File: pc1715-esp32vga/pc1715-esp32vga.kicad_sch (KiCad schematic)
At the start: 31 parts, among them J1001 IDC10_VIDEO_IN, J1002 VGAOUT, J1003 USB_B, J1004 KEYPAD, J1005 IDC16_VGAOUT, SW1001 RST, U1001 ESP32-S3-WROOM-1, U1002 LM1117MP-3.3

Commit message: Revision 2
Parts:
- removed D1001: 1N5819, Diode_THT:D_DO-41_SOD81_P7.62mm_Horizontal, symbol Diode:1N5819
- removed TP1001: TP_SPI, TestPoint:TestPoint_Pad_1.5x1.5mm, symbol Connector:TestPoint
- removed TP1002: TP_COPY, TestPoint:TestPoint_Pad_1.5x1.5mm, symbol Connector:TestPoint
- added D3: SYNC, LED_SMD:LED_1206_3216Metric_Pad1.42x1.75mm_HandSolder, symbol Device:LED
- added D4: STAT, LED_SMD:LED_1206_3216Metric_Pad1.42x1.75mm_HandSolder, symbol Device:LED
- added J6: USB_C_Receptacle_USB2.0_16P, Connector_USB:USB_C_Receptacle_GCT_USB4105-xx-A_16P_TopMnt_Horizontal, symbol Connector:USB_C_Receptacle_USB2.0_16P
- added J7: DBG, Connector_PinHeader_2.54mm:PinHeader_1x07_P2.54mm_Vertical, symbol Connector:Conn_01x07_Pin
- added R3, R4: 330, Resistor_SMD:R_0805_2012Metric_Pad1.20x1.40mm_HandSolder, symbol Device:R
- D1: renamed from D1002; value 1N5819 -> BAT54C Uf 0,24V; footprint Diode_THT:D_DO-41_SOD81_P7.62mm_Horizontal -> Package_TO_SOT_SMD:SOT-23; symbol Diode:1N5819 -> Diode:BAT54C
- D2: renamed from D1003; value LED -> 3V3
- J4: renamed from J1004; footprint Connector_PinHeader_2.54mm:PinHeader_1x05_P2.54mm_Vertical -> Connector_PinSocket_2.54mm:PinSocket_1x05_P2.54mm_Horizontal
- JP1: renamed from JP1001; footprint Connector_PinSocket_2.54mm:PinSocket_1x02_P2.54mm_Vertical -> Connector_PinHeader_2.54mm:PinHeader_1x02_P2.54mm_Vertical
- R2: renamed from R1001; value 300 -> 330
- renumbered C1001 to C1, C1002 to C2, J1001 to J1, J1002 to J2, J1003 to J3, J1005 to J5, R1010 to R1, R1009 to R10, R1002 to R11, R1003 to R12, R1011 to R13, R1004 to R5, R1005 to R6, R1006 to R7, R1007 to R8, R1008 to R9, SW1001 to SW1, U1002 to U1, U1001 to U2
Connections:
- net +5V: now also D1.3; no longer D1.1 (K)
- net BSYNC: now also J7.7 (Pin_7)
- net GND: now also J6.A1 (GND), J6.A12 (GND), J6.B1 (GND), J6.B12 (GND), J6.S1 (SHIELD), R3.1, R4.1
- net INTENS: now also J7.5 (Pin_5)
- net K_DOWN: now also J4.2 (Pin_2); no longer J4.4 (Pin_4)
- net K_LEFT: now also J4.5 (Pin_5); no longer J4.1 (Pin_1)
- net K_RIGHT: now also J4.1 (Pin_1); no longer J4.5 (Pin_5)
- net K_UP: now also J4.4 (Pin_4); no longer J4.2 (Pin_2)
- net USB_DN: now also J6.A7 (D-), J6.B7 (D-)
- net USB_DP: now also J6.A6 (D+), J6.B6 (D+)
- net VIDEO: now also J7.6 (Pin_6)
- net at U2.16 (GPIO46): now also D3.2 (A)
- net TP_11: now reaches U2.19 (GPIO11/TOUCH11/ADC2_CH0/FSPID/FSPIIO5/SUBSPID)
- net TP_11: now also J7.3 (Pin_3)
- net TP_12: now reaches U2.20 (GPIO12/TOUCH12/ADC2_CH1/FSPICLK/FSPIIO6/SUBSPICLK)
- net TP_12: now also J7.4 (Pin_4)
- net TP_SPI: now reaches U2.21 (GPIO13/TOUCH13/ADC2_CH2/FSPIQ/FSPIIO7/SUBSPIQ)
- net TP_SPI: now also J7.1 (Pin_1)
- net TP_CPY: now reaches U2.22 (GPIO14/TOUCH14/ADC2_CH3/FSPIWP/FSPIDQS/SUBSPIWP)
- net TP_CPY: now also J7.2 (Pin_2)
- net at U2.35 (MTMS/GPIO42): now also D4.2 (A)
- net VBUS: now reaches D1.2, J3.1 (VBUS)
- net VBUS: now also J6.A4 (VBUS), J6.A9 (VBUS), J6.B4 (VBUS), J6.B9 (VBUS)
- net 5V_VID: now reaches J1.1 (Pin_1), J1.2 (Pin_2)
- net 5V_VID: now also D1.1
- new net: D3.1 (K), R3.2
- new net: D4.1 (K), R4.2
- no-connect marks 26 -> 25
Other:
- note added: "Debugging"
- note removed: "A7100 PullUp *OPTIONAL* für PC1715 nicht benötigt"
- moved on the sheet: H1001, H1002, H1003, H1004, J1, J4, R11, R12, R13

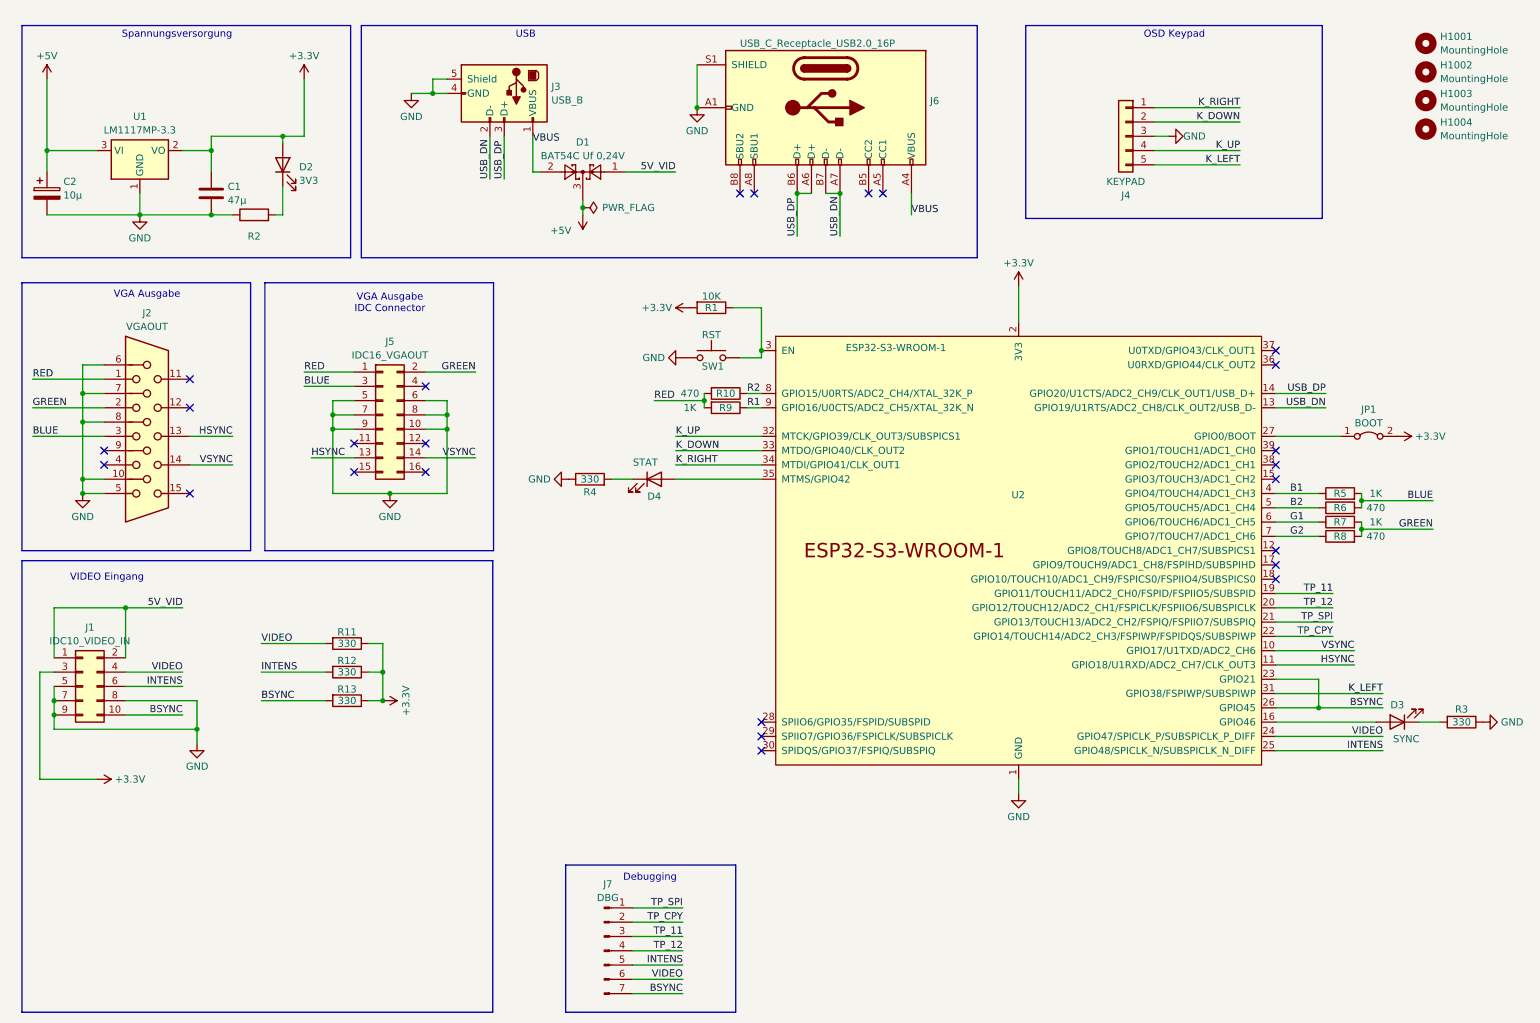
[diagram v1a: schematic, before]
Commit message: Rev 2 Main PCB with keypad
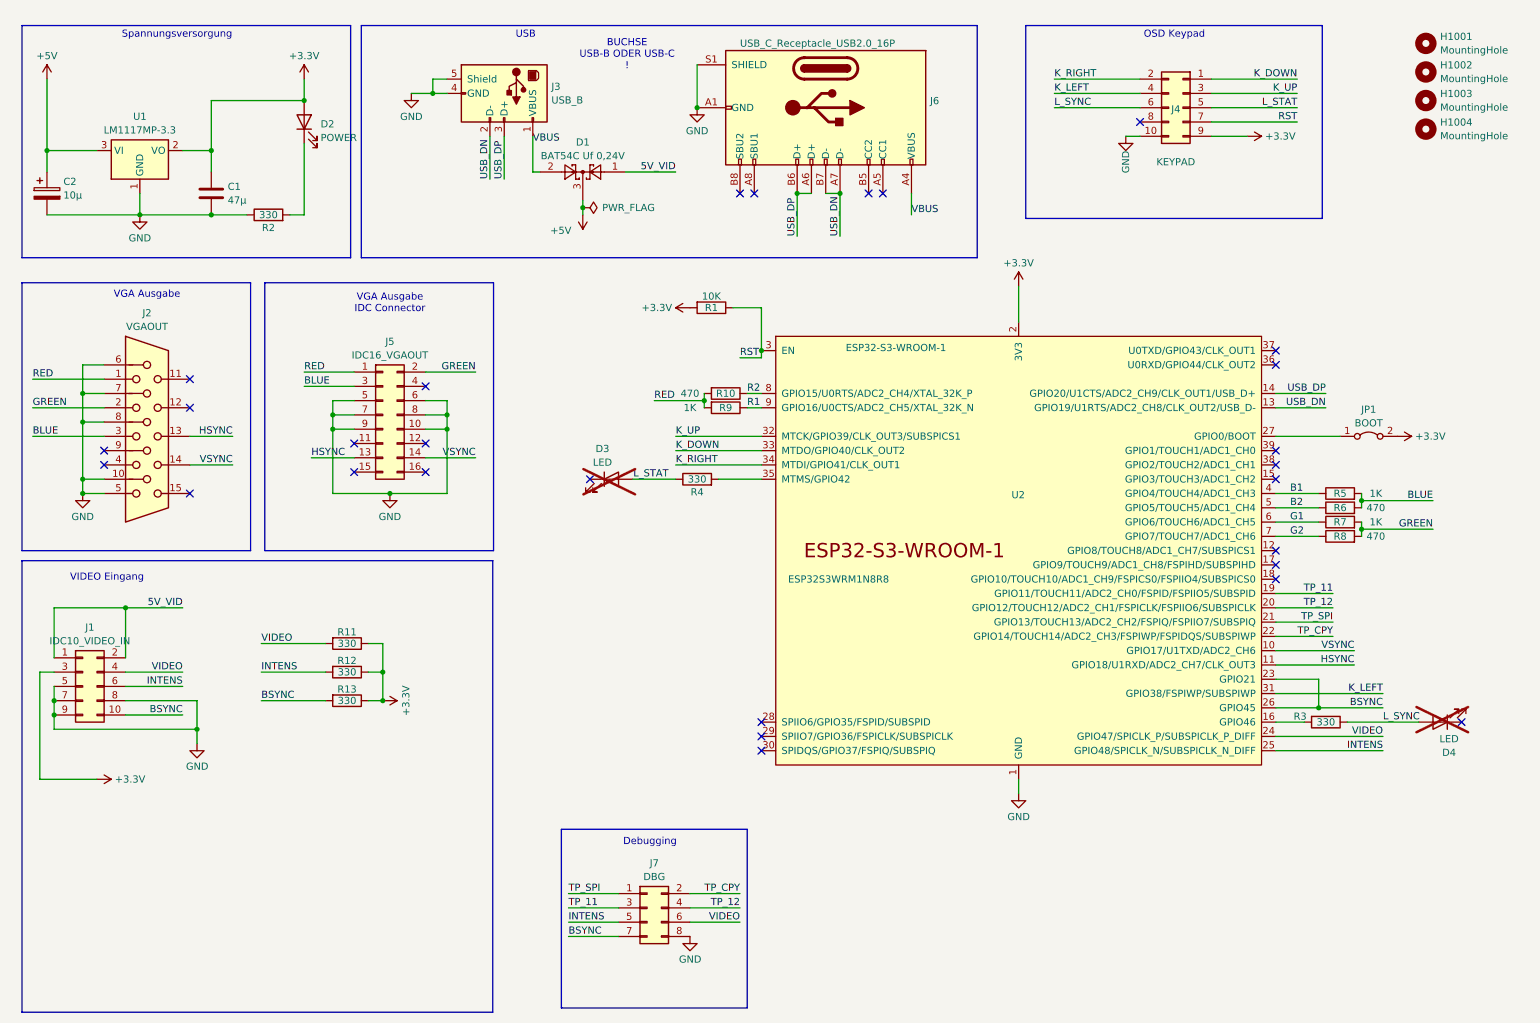
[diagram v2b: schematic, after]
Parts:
- removed SW1: RST, Button_Switch_SMD:SW_Push_1P1T_NO_6x6mm_H9.5mm, symbol Switch:SW_Push
- D2: value 3V3 -> POWER; footprint LED_SMD:LED_1206_3216Metric_Pad1.42x1.75mm_HandSolder -> Diode_SMD:D_0805_2012Metric_Pad1.15x1.40mm_HandSolder
- D3: value SYNC -> LED; footprint LED_SMD:LED_1206_3216Metric_Pad1.42x1.75mm_HandSolder -> (none); now not fitted; now left out of the parts list
- D4: value STAT -> LED; footprint LED_SMD:LED_1206_3216Metric_Pad1.42x1.75mm_HandSolder -> (none); now not fitted; now left out of the parts list
- J4: footprint Connector_PinSocket_2.54mm:PinSocket_1x05_P2.54mm_Horizontal -> Connector_IDC:IDC-Header_2x05_P2.54mm_Vertical; symbol Connector_Generic:Conn_01x05 -> Connector_Generic:Conn_02x05_Odd_Even
- J7: footprint Connector_PinHeader_2.54mm:PinHeader_1x07_P2.54mm_Vertical -> Connector_PinHeader_2.54mm:PinHeader_2x04_P2.54mm_Vertical; symbol Connector:Conn_01x07_Pin -> Connector_Generic:Conn_02x04_Odd_Even
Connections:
- net +3.3V: now also J4.9 (Pin_9)
- net GND: now also J4.10 (Pin_10), J7.8 (Pin_8); no longer J4.3 (Pin_3), R3.1, R4.1
- net K_DOWN: now also J4.1 (Pin_1); no longer J4.2 (Pin_2)
- net K_LEFT: now also J4.4 (Pin_4); no longer J4.5 (Pin_5)
- net K_RIGHT: now also J4.2 (Pin_2); no longer J4.1 (Pin_1)
- net K_UP: now also J4.3 (Pin_3); no longer J4.4 (Pin_4)
- net at U2.16 (GPIO46): now also R3.2; no longer D3.2 (A)
- net RST: now reaches R1.1, U2.3 (EN)
- net RST: now also J4.7 (Pin_7)
- net at U2.35 (MTMS/GPIO42): now also R4.2; no longer D4.2 (A)
- net at D3.1 (K): no longer R3.2
- net at D4.1 (K): no longer R4.2
- new net L_STAT: D3.2 (A), J4.5 (Pin_5), R4.1
- new net L_SYNC: D4.2 (A), J4.6 (Pin_6), R3.1
- no-connect marks 25 -> 28
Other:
- note added: "BUCHSE USB-B ODER USB-C !"
- moved on the sheet: R2, R3, R4

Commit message: Silkscreen correction for J4 Changed BOOT jumper to PROG jumper, Connection to GND instead VCC
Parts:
- JP1: value BOOT -> PROG
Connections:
- net +3.3V: no longer JP1.2 (B)
- net GND: now also JP1.2 (B)
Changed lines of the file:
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@@
-	)
-	(symbol
-		(lib_id "power:+3.3V")
-		(at 261.62 90.17 270)
-		(unit 1)
-		(exclude_from_sim no)
-		(in_bom yes)
-		(on_board yes)
-		(dnp no)
-		(fields_autoplaced yes)
-		(property "Reference" "#PWR01004"
-			(at 257.81 90.17 0)
-			(effects
-				(font
-					(size 1.27 1.27)
-				)
-				(hide yes)
-			)
-		)
-		(property "Value" "+3.3V"
-			(at 264.795 90.17 90)
-			(effects
-				(font
-					(size 1.27 1.27)
-				)
-				(justify left)
-			)
-		)
-		(property "Footprint" ""
-			(at 261.62 90.17 0)
-			(effects
-				(font
-					(size 1.27 1.27)
-				)
-				(hide yes)
-			)
-		)
-		(property "Datasheet" ""
-			(at 261.62 90.17 0)
-			(effects
-				(font
-					(size 1.27 1.27)
-				)
-				(hide yes)
-			)
-		)
-		(property "Description" "Power symbol creates a global label with name \"+3.3V\""
-			(at 261.62 90.17 0)
-			(effects
-				(font
-					(size 1.27 1.27)
-				)
-				(hide yes)
-			)
-		)
-		(pin "1"
-		)
-		(instances
-			(project "pc1715-esp32vga"
-				(path "/341c8b8e-dd99-4606-bdc6-0ff6680aa4f8"
-					(reference "#PWR01004")
-					(unit 1)
-				)
-			)
-		)
 	)
 	(symbol
@@
 	)
 	(symbol
+		(lib_id "power:GND")
+		(at 261.62 90.17 0)
+		(unit 1)
+		(exclude_from_sim no)
+		(in_bom yes)
+		(on_board yes)
+		(dnp no)
+		(property "Reference" "#PWR02"
+			(at 261.62 96.52 0)
+			(effects
+				(font
+					(size 1.27 1.27)
+				)
+				(hide yes)
+			)
+		)
+		(property "Value" "GND"
+			(at 261.62 94.742 90)
+			(effects
+				(font
+					(size 1.27 1.27)
+				)
+			)
+		)
+		(property "Footprint" ""
+			(at 261.62 90.17 0)
+			(effects
+				(font
+					(size 1.27 1.27)
+				)
+				(hide yes)
+			)
+		)
+		(property "Datasheet" ""
+			(at 261.62 90.17 0)
+			(effects
+				(font
+					(size 1.27 1.27)
+				)
+				(hide yes)
+			)
+		)
+		(property "Description" "Power symbol creates a global label with name \"GND\" , ground"
+			(at 261.62 90.17 0)
+			(effects
+				(font
+					(size 1.27 1.27)
+				)
+				(hide yes)
+			)
+		)
+		(pin "1"
+		)
+		(instances
+			(project "pc1715-esp32vga"
+				(path "/341c8b8e-dd99-4606-bdc6-0ff6680aa4f8"
+					(reference "#PWR02")
+					(unit 1)
+				)
+			)
+		)
+	)
+	(symbol
 		(lib_id "power:+3.3V")
 		(at 194.31 63.5 0)
@@
 			)
 		)
-		(property "Value" "BOOT"
+		(property "Value" "PROG"
 			(at 256.54 87.8148 0)
 			(effects

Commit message: Update to rev3
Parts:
- removed D1: BAT54C Uf 0,24V, Package_TO_SOT_SMD:SOT-23, symbol Diode:BAT54C
- added D4, D5, D6: SD103BW, Diode_SMD:D_SOD-123, symbol Device:D
- added J8: EXT-5V, Connector_PinHeader_2.54mm:PinHeader_1x02_P2.54mm_Vertical, symbol Connector:Conn_01x02_Pin
- added JP2: Jumper_3_Open, Jumper:SolderJumper-3_P1.3mm_Open_RoundedPad1.0x1.5mm_NumberLabels, symbol Jumper:Jumper_3_Open
- added JP3: USB-VIN, Connector_PinHeader_2.54mm:PinHeader_1x03_P2.54mm_Vertical, symbol Connector:Conn_01x03_Pin
- H1001, H1002, H1003, H1004: symbol Mechanical:MountingHole -> Mechanical:MountingHole_Pad
- J2: symbol Connector:DE15_Receptacle_HighDensity -> Connector:DE15_Socket_HighDensity_MountingHoles
- J7, JP1: now not fitted
- renumbered D2 to D1, D3 to D2, D4 to D3
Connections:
- net +5V: now also J8.1 (Pin_1), JP2.2 (C), JP3.2 (Pin_2)
- net 5V_VID: now also JP2.3 (B), JP3.3 (Pin_3)
- net BSYNC: now also D6.2 (A); no longer J1.10 (Pin_10)
- net GND: now also H1001.1, H1002.1, H1003.1, H1004.1, J2.0, J8.2 (Pin_2)
- net INTENS: now also D5.2 (A); no longer J1.6 (Pin_6)
- net VBUS: now also JP2.1 (A), JP3.1 (Pin_1)
- net VIDEO: now also D4.2 (A); no longer J1.4 (Pin_4)
- new net: D6.1 (K), J1.10 (Pin_10)
- new net: D4.1 (K), J1.4 (Pin_4)
- new net: D5.1 (K), J1.6 (Pin_6)
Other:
- moved on the sheet: C1, C2, D1, J1, J3, J4, J5, J6, R1, R11, R12, R13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
